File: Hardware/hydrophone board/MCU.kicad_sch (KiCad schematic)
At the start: 2 parts, among them J401 Conn_01x07, U401 DEV-16771

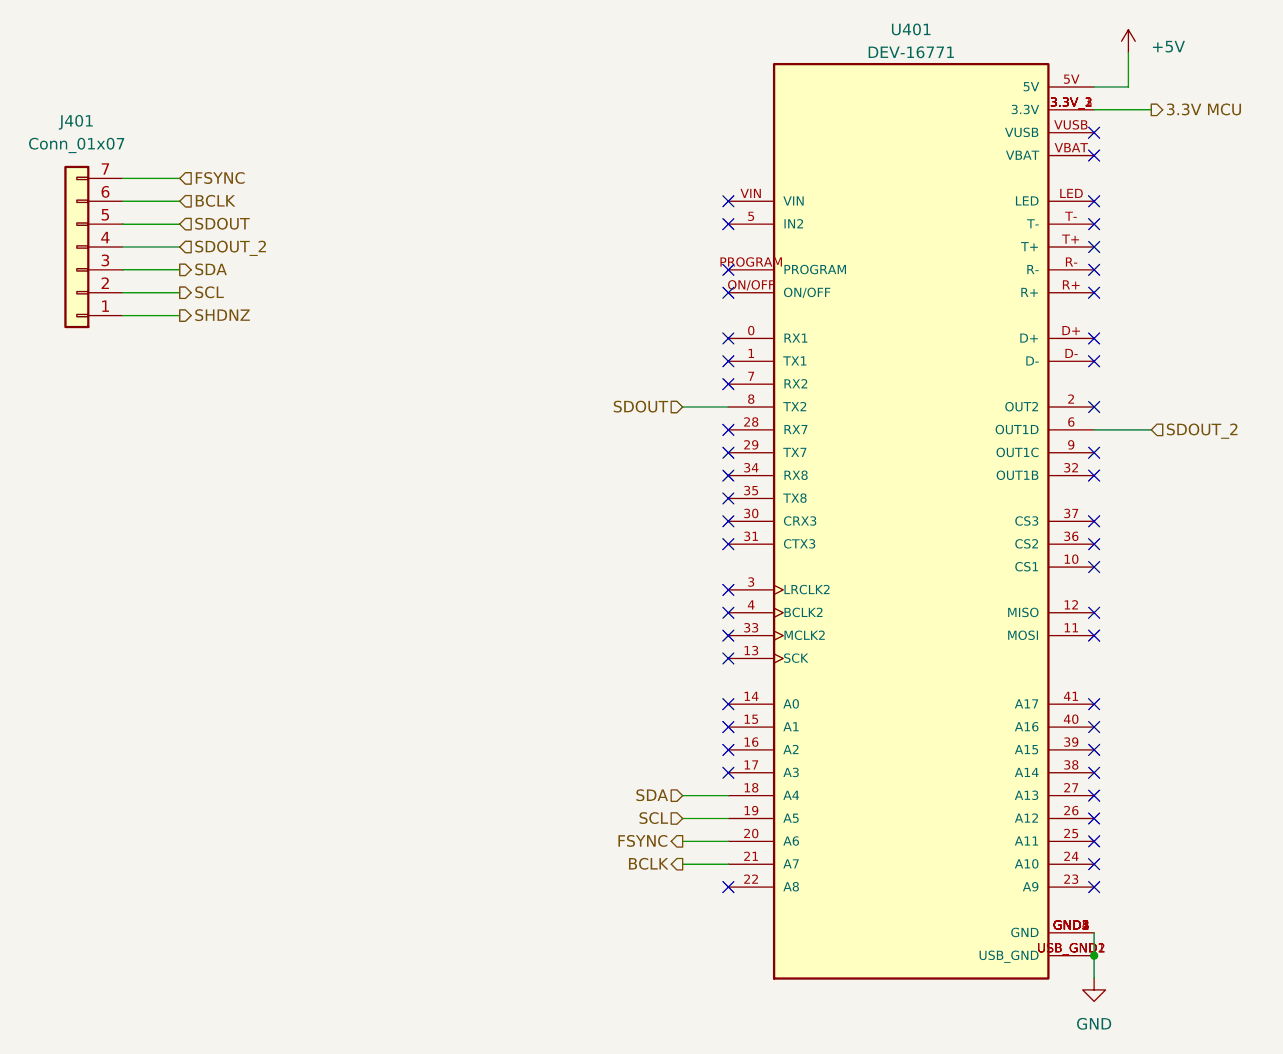
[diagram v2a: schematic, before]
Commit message: changed 5V pin
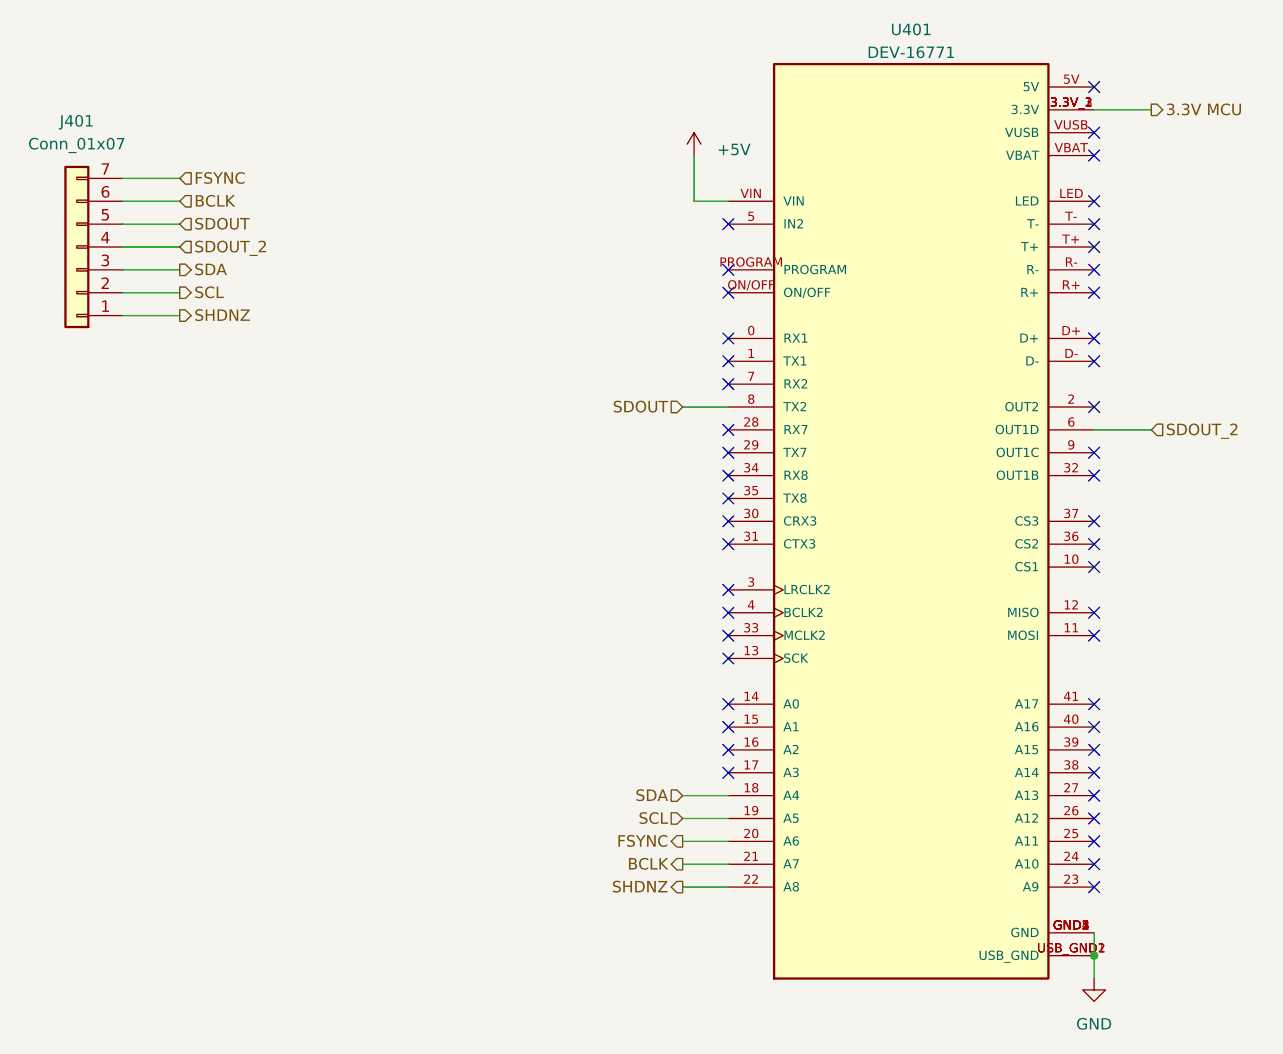
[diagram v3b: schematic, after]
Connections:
- net +5V: now also U401.VIN; no longer U401.5V
- net SHDNZ: now also U401.22 (A8)
- no-connect marks 48 -> 47
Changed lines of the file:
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@@
   (no_connect (at 187.96 55.88))
   (no_connect (at 147.32 83.82))
+  (no_connect (at 187.96 40.64))
   (no_connect (at 147.32 109.22))
   (no_connect (at 147.32 73.66))
@@
   (no_connect (at 187.96 116.84))
   (no_connect (at 147.32 81.28))
-  (no_connect (at 147.32 53.34))
   (no_connect (at 187.96 53.34))
   (no_connect (at 147.32 88.9))
@@
   (no_connect (at 187.96 58.42))
   (no_connect (at 147.32 78.74))
-  (no_connect (at 147.32 129.54))
   (no_connect (at 187.96 68.58))
   (no_connect (at 187.96 129.54))
@@
     (stroke (width 0) (type default))
   )
+  (wire (pts (xy 143.51 53.34) (xy 143.51 48.26))
+    (stroke (width 0) (type default))
+  )
   (wire (pts (xy 80.01 55.88) (xy 86.36 55.88))
     (stroke (width 0) (type default))
@@
     (stroke (width 0) (type default))
   )
-  (wire (pts (xy 191.77 40.64) (xy 187.96 40.64))
-    (stroke (width 0) (type default))
-  )
   (wire (pts (xy 142.24 124.46) (xy 147.32 124.46))
     (stroke (width 0) (type default))
@@
     (stroke (width 0) (type default))
   )
-  (wire (pts (xy 191.77 36.83) (xy 191.77 40.64))
+  (wire (pts (xy 142.24 129.54) (xy 147.32 129.54))
     (stroke (width 0) (type default))
   )
@@
     (stroke (width 0) (type default))
   )
+  (wire (pts (xy 143.51 53.34) (xy 147.32 53.34))
+    (stroke (width 0) (type default))
+  )
   (wire (pts (xy 142.24 121.92) (xy 147.32 121.92))
     (stroke (width 0) (type default))
@@
   )
   (hierarchical_label "BCLK" (shape output) (at 142.24 127 180) (fields_autoplaced)
+    (effects (font (size 1.27 1.27)) (justify right))
+  )
+  (hierarchical_label "SHDNZ" (shape output) (at 142.24 129.54 180) (fields_autoplaced)
     (effects (font (size 1.27 1.27)) (justify right))
   )
@@
     )
   )
+  (symbol (lib_id "power:+5V") (at 143.51 48.26 0) (unit 1)
+    (in_bom yes) (on_board yes) (dnp no) (fields_autoplaced)
+    (property "Reference" "#PWR032" (at 143.51 52.07 0)
+      (effects (font (size 1.27 1.27)) hide)
+    )
+    (property "Value" "+5V" (at 146.05 47.625 0)
+      (effects (font (size 1.27 1.27)) (justify left))
+    )
+    (property "Footprint" "" (at 143.51 48.26 0)
+      (effects (font (size 1.27 1.27)) hide)
+    )
+    (property "Datasheet" "" (at 143.51 48.26 0)
+      (effects (font (size 1.27 1.27)) hide)
+    )
+    (pin "1")
+    (instances
+      (project "hydrophone board"
+        (path "/4356d3a6-6a00-447d-897e-473f60221539/cf9d259f-9643-49eb-8aca-1ca8b75f4d64"
+          (reference "#PWR032") (unit 1)
+        )
+        (path "/4356d3a6-6a00-447d-897e-473f60221539/1c2c9d85-5695-48de-99af-3ac5f27a43fe"
+          (reference "#PWR0260") (unit 1)
+        )
+      )
+    )
+  )
   (symbol (lib_id "PCM_4ms_Power-symbol:GND") (at 187.96 139.7 0) (unit 1)
     (in_bom yes) (on_board yes) (dnp no) (fields_autoplaced)
@@
         )
       )
-    )
-  )
-  (symbol (lib_id "power:+5V") (at 191.77 36.83 0) (unit 1)
-    (in_bom yes) (on_board yes) (dnp no) (fields_autoplaced)
-    (property "Reference" "#PWR032" (at 191.77 40.64 0)
-      (effects (font (size 1.27 1.27)) hide)
-    )
-    (property "Value" "+5V" (at 194.31 36.195 0)
-      (effects (font (size 1.27 1.27)) (justify left))
-    )
-    (property "Footprint" "" (at 191.77 36.83 0)
-      (effects (font (size 1.27 1.27)) hide)
-    )
-    (property "Datasheet" "" (at 191.77 36.83 0)
-      (effects (font (size 1.27 1.27)) hide)
-    )
-    (pin "1")
-    (instances
-      (project "hydrophone board"
-        (path "/4356d3a6-6a00-447d-897e-473f60221539/cf9d259f-9643-49eb-8aca-1ca8b75f4d64"
-          (reference "#PWR032") (unit 1)
-        )
-        (path "/4356d3a6-6a00-447d-897e-473f60221539/1c2c9d85-5695-48de-99af-3ac5f27a43fe"
-          (reference "#PWR0401") (unit 1)
-        )
-      )
